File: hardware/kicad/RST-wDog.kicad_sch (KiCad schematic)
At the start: 6 parts, among them Q4 2N3904, U4 ATtiny13A-P

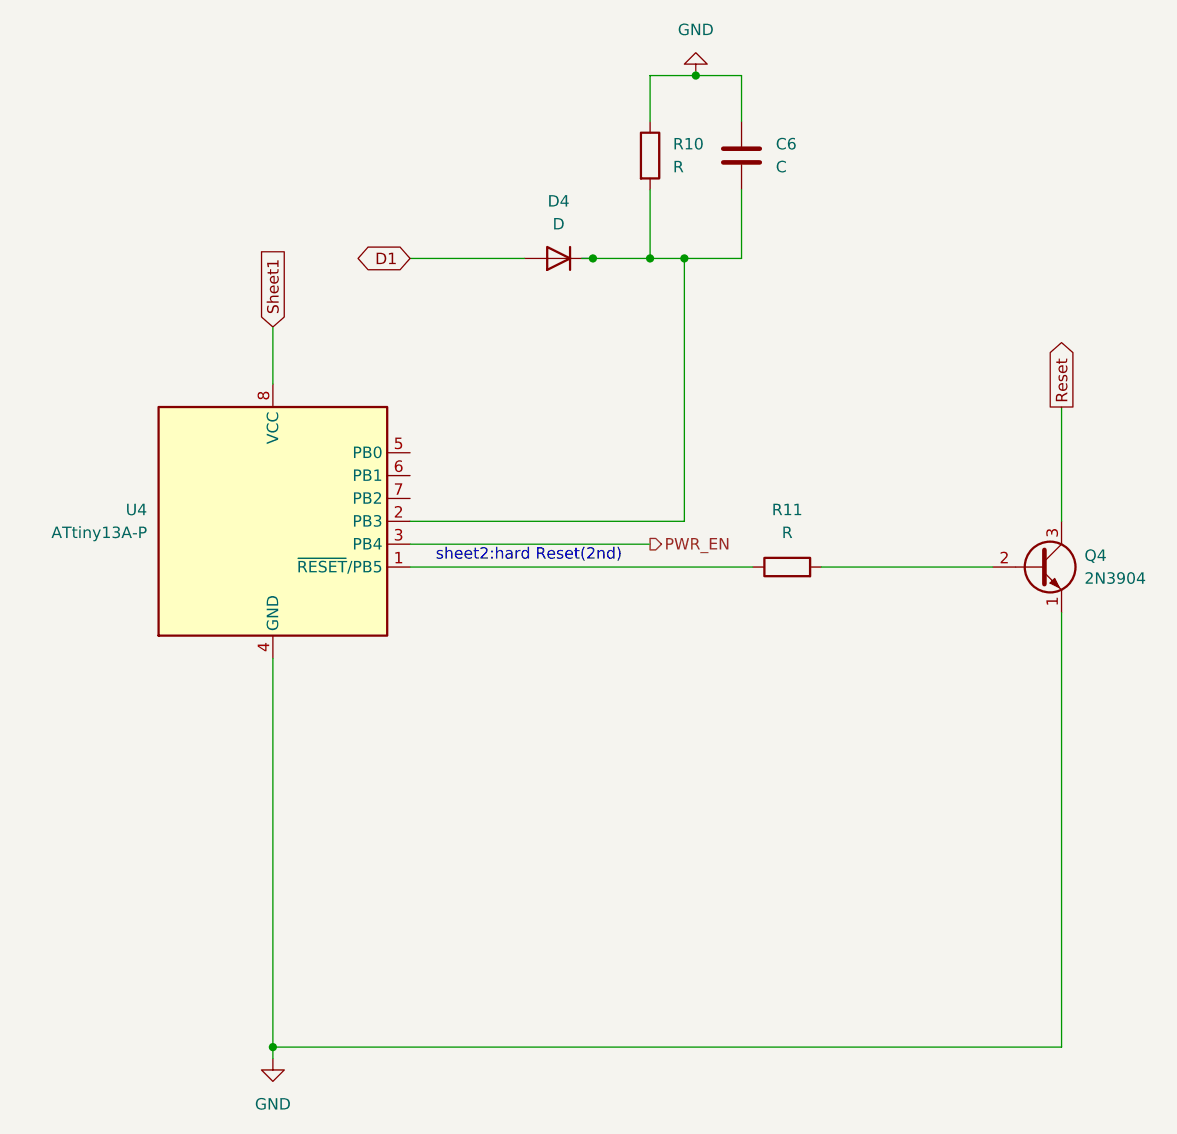
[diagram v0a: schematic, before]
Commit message: chore: KiCad 회로도 최신 변경사항 반영
원본 작업 폴더가 "회로도 편집 완료/20260901_ver01"로 재구성됨(이전 smartvault-pcb-1
경로는 더 이상 존재하지 않음). 하위 시트 6개 전부와 최상위 시트에 실제 설계 변경
있음(DoorRock-drv는 축소, 최상위 시트는 대폭 확장 — 회로가 재구성된 것으로 보임).
PCB 레이아웃 자체는 변경 없음. footprint.xlsx(부품-풋프린트 매핑) 신규 추가.

파일 내부의 프로젝트명 자기참조는 원본 작업 파일명("20260901_ver01")이 아니라
저장소 표준 이름("smartvault")으로 맞춰서 복사 — 작업 폴더 쪽 날짜/버전 파일명
관례를 저장소까지 끌고 오지 않음(git이 버전을 관리).

s_vault.kicad_sym(커스텀 심볼 라이브러리)은 원본 경로에서 찾지 못해 갱신 못함 —
RS485-com/power 시트가 이 라이브러리를 참조하므로, 최신 심볼이 바뀌었다면 다음에
갱신 필요(hardware/README.md에 기록해둠).

Co-Authored-By: Claude Sonnet 5 <noreply@anthropic.com>
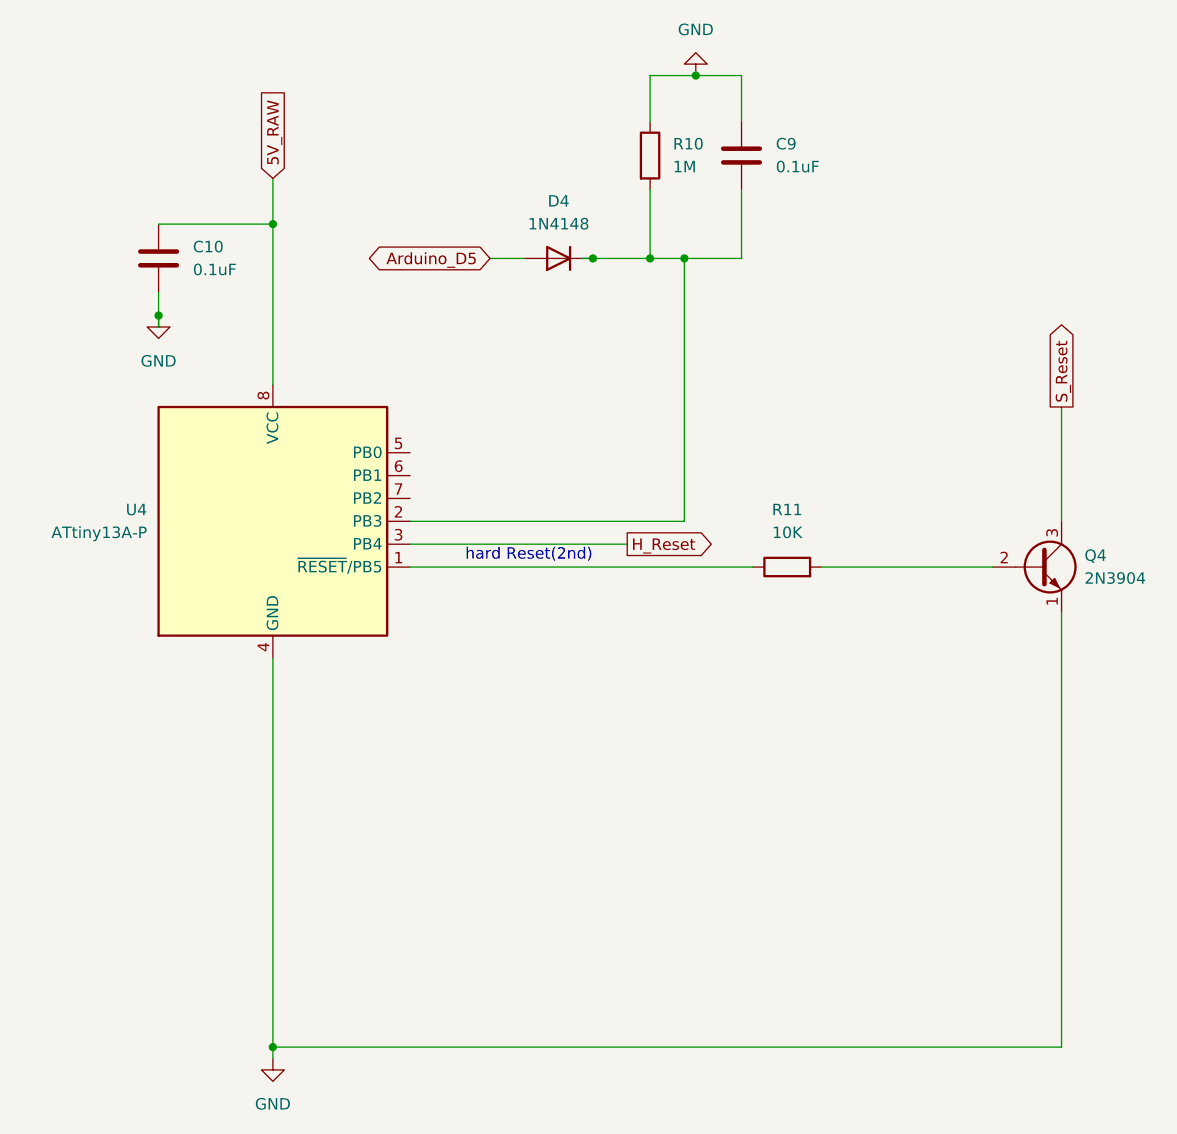
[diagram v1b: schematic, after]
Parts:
- added C10: 0.1uF, Capacitor_SMD:C_0805_2012Metric, symbol Device:C
- C9: renamed from C6; value C -> 0.1uF; footprint (none) -> Capacitor_SMD:C_0805_2012Metric
- D4: value D -> 1N4148; footprint (none) -> Diode_SMD:D_SOD-123
- Q4: footprint Package_TO_SOT_THT:TO-92_Inline -> Package_TO_SOT_SMD:SOT-23
- R10: value R -> 1M; footprint (none) -> Resistor_SMD:R_0805_2012Metric
- R11: value R -> 10K; footprint (none) -> Resistor_SMD:R_0805_2012Metric
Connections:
- net GND: now also C10.2
- net D1 renamed Arduino_D5
- net PWR_EN renamed H_Reset
- net Reset renamed S_Reset
- net Sheet1 renamed 5V_RAW
- net 5V_RAW: now also C10.1
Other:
- note added: "hard Reset(2nd)"
- note removed: "sheet2:hard Reset(2nd)"
